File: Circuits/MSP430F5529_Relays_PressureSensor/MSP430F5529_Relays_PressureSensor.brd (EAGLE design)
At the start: 107.9 x 69.8 mm, 16 parts, among them K1 AQV21SMD, K2 AQV21SMD, U2 SSCMRNN015PA3A3

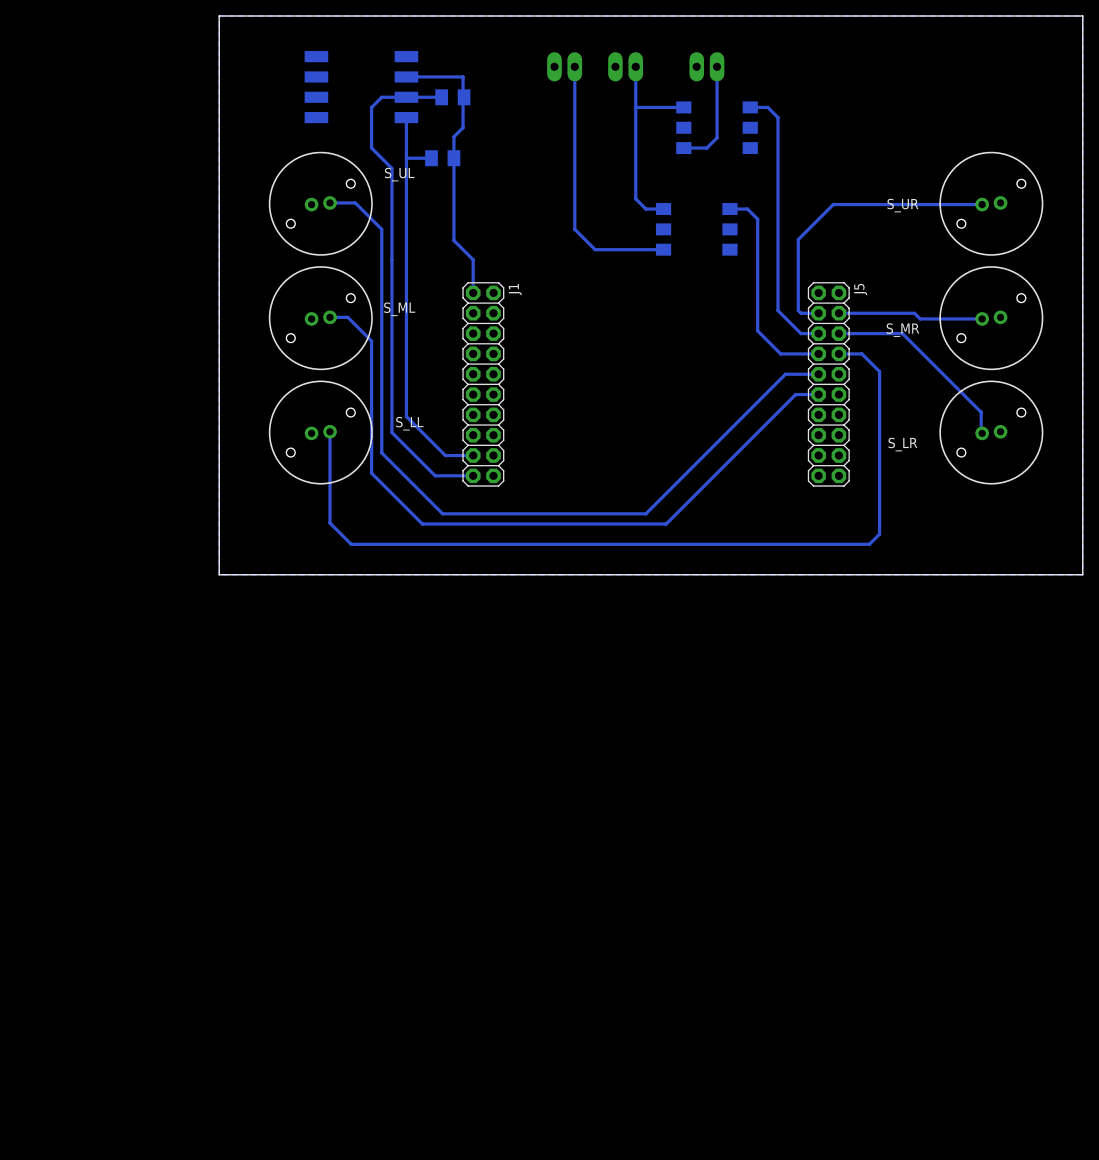
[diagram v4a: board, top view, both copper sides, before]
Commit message: Add power supply and connector for GUI_Switches board
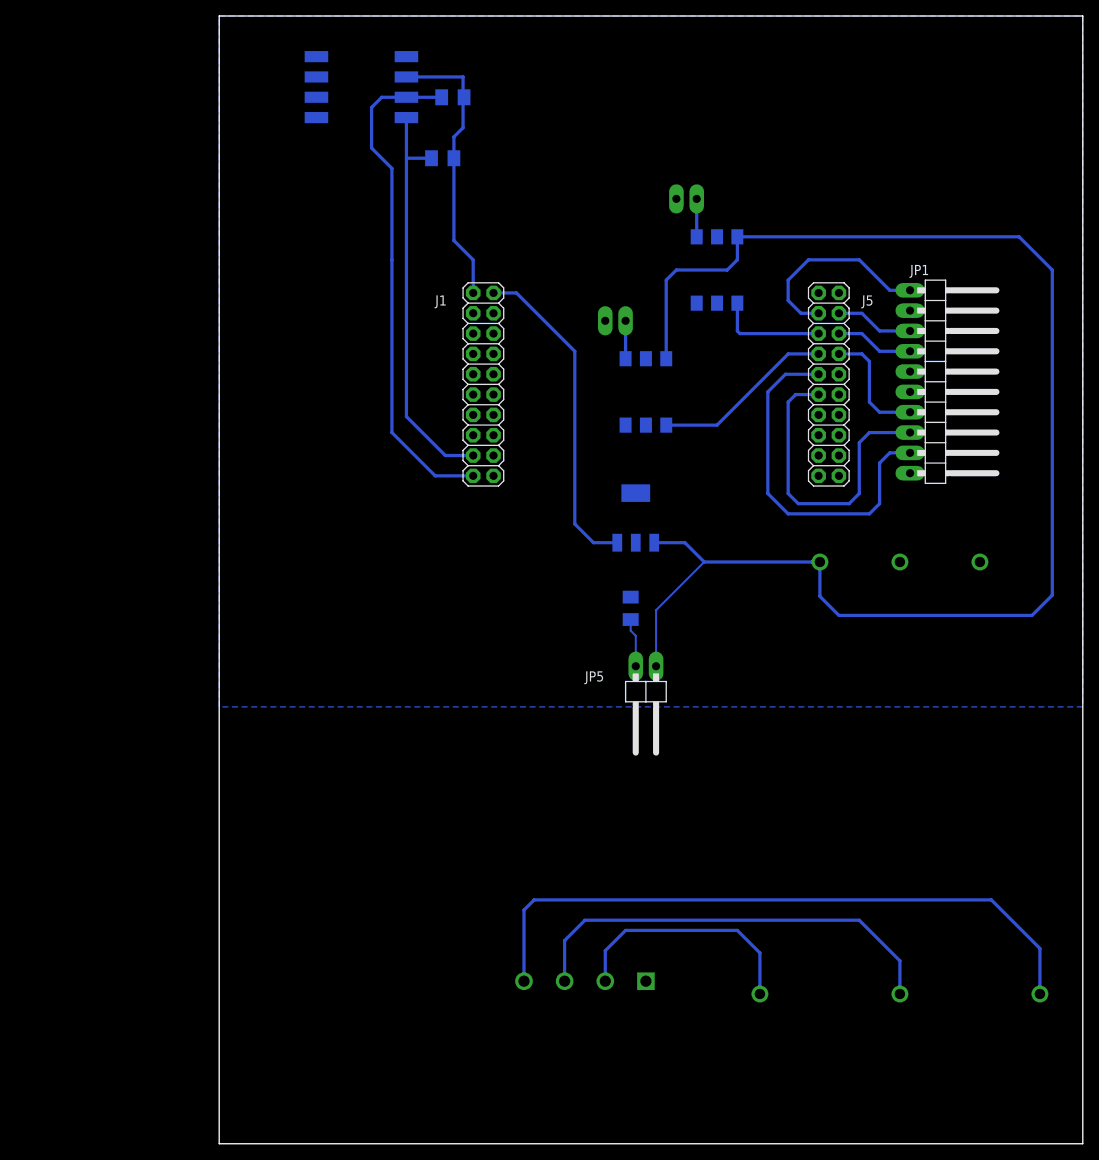
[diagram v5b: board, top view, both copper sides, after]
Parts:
- removed S_LL, S_LR, S_ML, S_MR, S_UL, S_UR: K12C15N, SamacSys_Parts:K12C15N
- added IC1: UA78M05DCY, linear:SOT223
- added J2: OSTTG0451XBNO_THP, MasterSPIS:TERM_4PIN_5.08MM_NO_THP
- added JP5: LED, pinhead:1X02/90
- added PS1: YW1515ATHP, MasterSPIS:YW15
- added R3: 2k, resistor:M1206
- JP1: value RelayPower -> (none); device pinhead:1X02/90 -> pinhead:1X10/90
- moved JP1 58.4 mm to (64.8, 24.1), flipped to the top, turned to 270 degrees
- moved JP2 32.4 mm to (24.1, 35.6)
- moved K1 21.3 mm to (27.9, 22.9), turned to 0 degrees
- moved K2 17.8 mm to (36.8, 38.1), turned to 0 degrees
- moved JP3 16.7 mm to (33.0, 50.8)
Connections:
- new net AC_L: J2.P2, PS1.P3
- new net AC_N: J2.P3, PS1.P2
- new net FG: J2.P4, PS1.P1
- new net N$1: JP5.2, R3.2
- new net V-: PS1.P6
- net 12V: now also IC1.1, JP5.1, PS1.P4; no longer JP1.1
- net 5V: now also IC1.3
- net GND: now also IC1.2, IC1.4, JP1.10, JP1.5, JP1.6, PS1.P5, R3.1; no longer S_LL.1, S_LR.1, S_ML.1, S_MR.1, S_UL.1, S_UR.1
- net P1.2: now also JP1.8; no longer S_ML.2
- net P1.3: now also JP1.9; no longer S_UL.2
- net P2.0: now also JP1.3; no longer S_MR.2
- net P2.2: now also JP1.4; no longer S_LR.2
- net P2.4: now also JP1.1; no longer S_UR.2
- net P7.4: now also JP1.7; no longer S_LL.2
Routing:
- net 12V: track 26.5 -> 177.0 mm
- net P7.4: track 108.1 -> 14.9 mm
- net FG: track 0.00 -> 82.1 mm
- net P1.3: track 100.8 -> 44.9 mm
- net AC_N: track 0.00 -> 54.3 mm
- net P1.2: track 88.2 -> 38.8 mm
- net 5V: track 0.00 -> 41.0 mm
- net AC_L: track 0.00 -> 30.5 mm
- net INFLATE_PWR: track 32.5 -> 4.74 mm
- net P1.5: track 34.4 -> 13.8 mm
- net P2.2: track 24.5 -> 9.81 mm
- net P2.4: track 36.4 -> 24.9 mm
- net DEFLATE_PWR: track 13.6 -> 4.74 mm
- net P2.0: track 18.2 -> 9.81 mm
- net N$1: track 0.00 -> 6.10 mm
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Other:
- board size 107.9 x 69.8 mm -> 107.9 x 141 mm

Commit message: add mounting holes
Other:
- board size 107.9 x 141 mm -> 107.9 x 134.6 mm
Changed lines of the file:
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@@
 <layer number="43" name="vRestrict" color="2" fill="10" visible="yes" active="yes"/>
 <layer number="44" name="Drills" color="7" fill="1" visible="no" active="yes"/>
-<layer number="45" name="Holes" color="7" fill="1" visible="no" active="yes"/>
+<layer number="45" name="Holes" color="7" fill="1" visible="yes" active="yes"/>
 <layer number="46" name="Milling" color="3" fill="1" visible="no" active="yes"/>
 <layer number="47" name="Measures" color="7" fill="1" visible="no" active="yes"/>
@@
 <board>
 <plain>
-<wire x1="-25.4" y1="-71.12" x2="82.55" y2="-71.12" width="0" layer="20"/>
-<wire x1="82.55" y1="-71.12" x2="82.55" y2="69.85" width="0" layer="20"/>
+<wire x1="-25.4" y1="-64.77" x2="82.55" y2="-64.77" width="0" layer="20"/>
+<wire x1="82.55" y1="-64.77" x2="82.55" y2="69.85" width="0" layer="20"/>
 <wire x1="82.55" y1="69.85" x2="-25.4" y2="69.85" width="0" layer="20"/>
-<wire x1="-25.4" y1="69.85" x2="-25.4" y2="-71.12" width="0" layer="20"/>
+<wire x1="-25.4" y1="69.85" x2="-25.4" y2="-64.77" width="0" layer="20"/>
+<hole x="-19.05" y="63.5" drill="3.302"/>
+<hole x="76.2" y="63.5" drill="3.302"/>
+<hole x="76.2" y="-60.325" drill="3.302"/>
+<hole x="-19.05" y="-60.325" drill="3.302"/>
 </plain>
 <attributes>
